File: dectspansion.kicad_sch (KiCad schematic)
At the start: 21 parts, among them J1 Hexpansion-Connector, J2 Conn_02x10_Odd_Even, J3 AudioJack4, U2 SC14CVMDECT

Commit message: Created PCB layout
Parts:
- removed D1: LED, LED_SMD:LED_0805_2012Metric, symbol Device:LED
- removed J2: Conn_02x10_Odd_Even, Connector_PinHeader_2.54mm:PinHeader_2x10_P2.54mm_Vertical, symbol Connector_Generic:Conn_02x10_Odd_Even
- removed R1: R, Resistor_SMD:R_0603_1608Metric, symbol Device:R
- renumbered D2 to D3
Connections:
- net 3V3 is gone; now on net +3V3: J1.15 (3V3), J1.16 (3V3)
- net HS_H: now also U2.47 (URX)
- net HS_I: now also U2.48 (UTX)
- net Mic: now also R10.1; no longer R10.2
- net at U2.7 (VREFp): now also R10.2; no longer R10.1
- net LS_A: no longer names the net of J1.2 (LS_A)
- net LS_B: no longer names the net of J1.3 (LS_B)
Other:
- moved on the sheet: C11, C12, C4, C5, C6, C9, D2, D3, J1, J3, JP1, R10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

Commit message: Created PCB layout
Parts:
- added J2: Conn_01x03_Pin, Connector_PinHeader_2.54mm:PinHeader_1x03_P2.54mm_Vertical, symbol Connector:Conn_01x03_Pin
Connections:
- net GND: now also J2.3 (Pin_3)
- net HS_H: now also J2.2 (Pin_2)
- net HS_I: now also J2.1 (Pin_1)
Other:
- moved on the sheet: J1

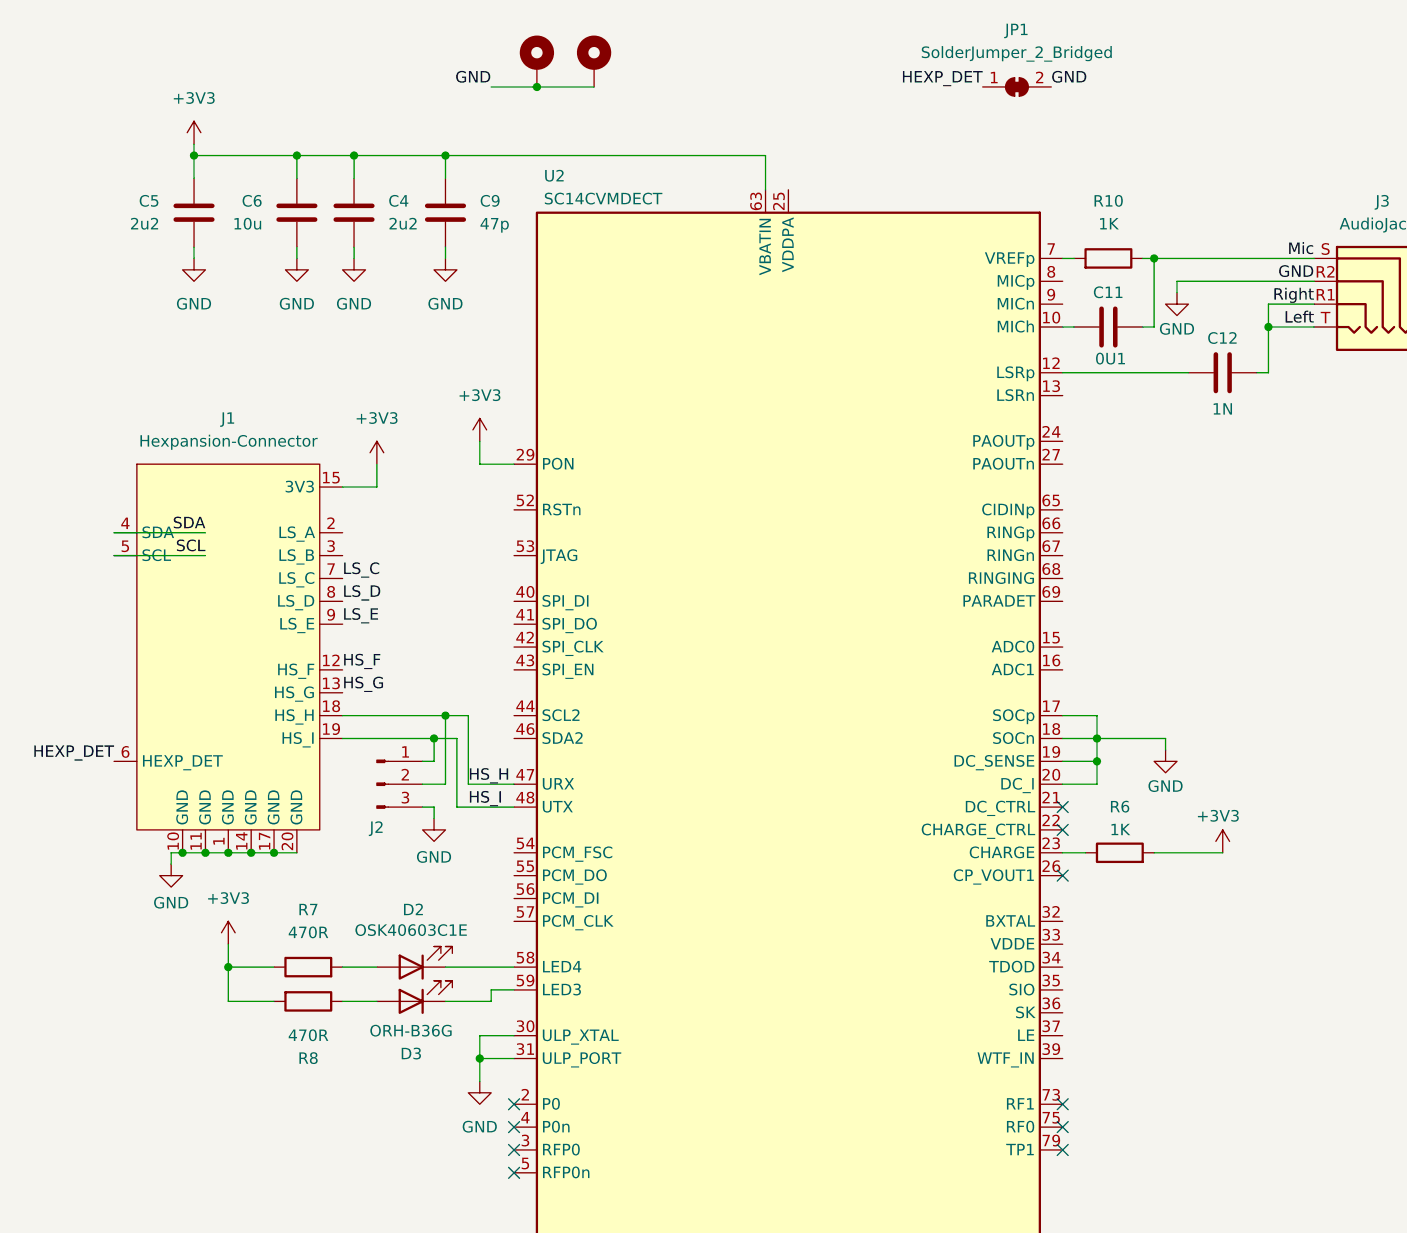
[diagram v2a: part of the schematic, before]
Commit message: Adjustments to schmatic, board layout, and added part list to readme
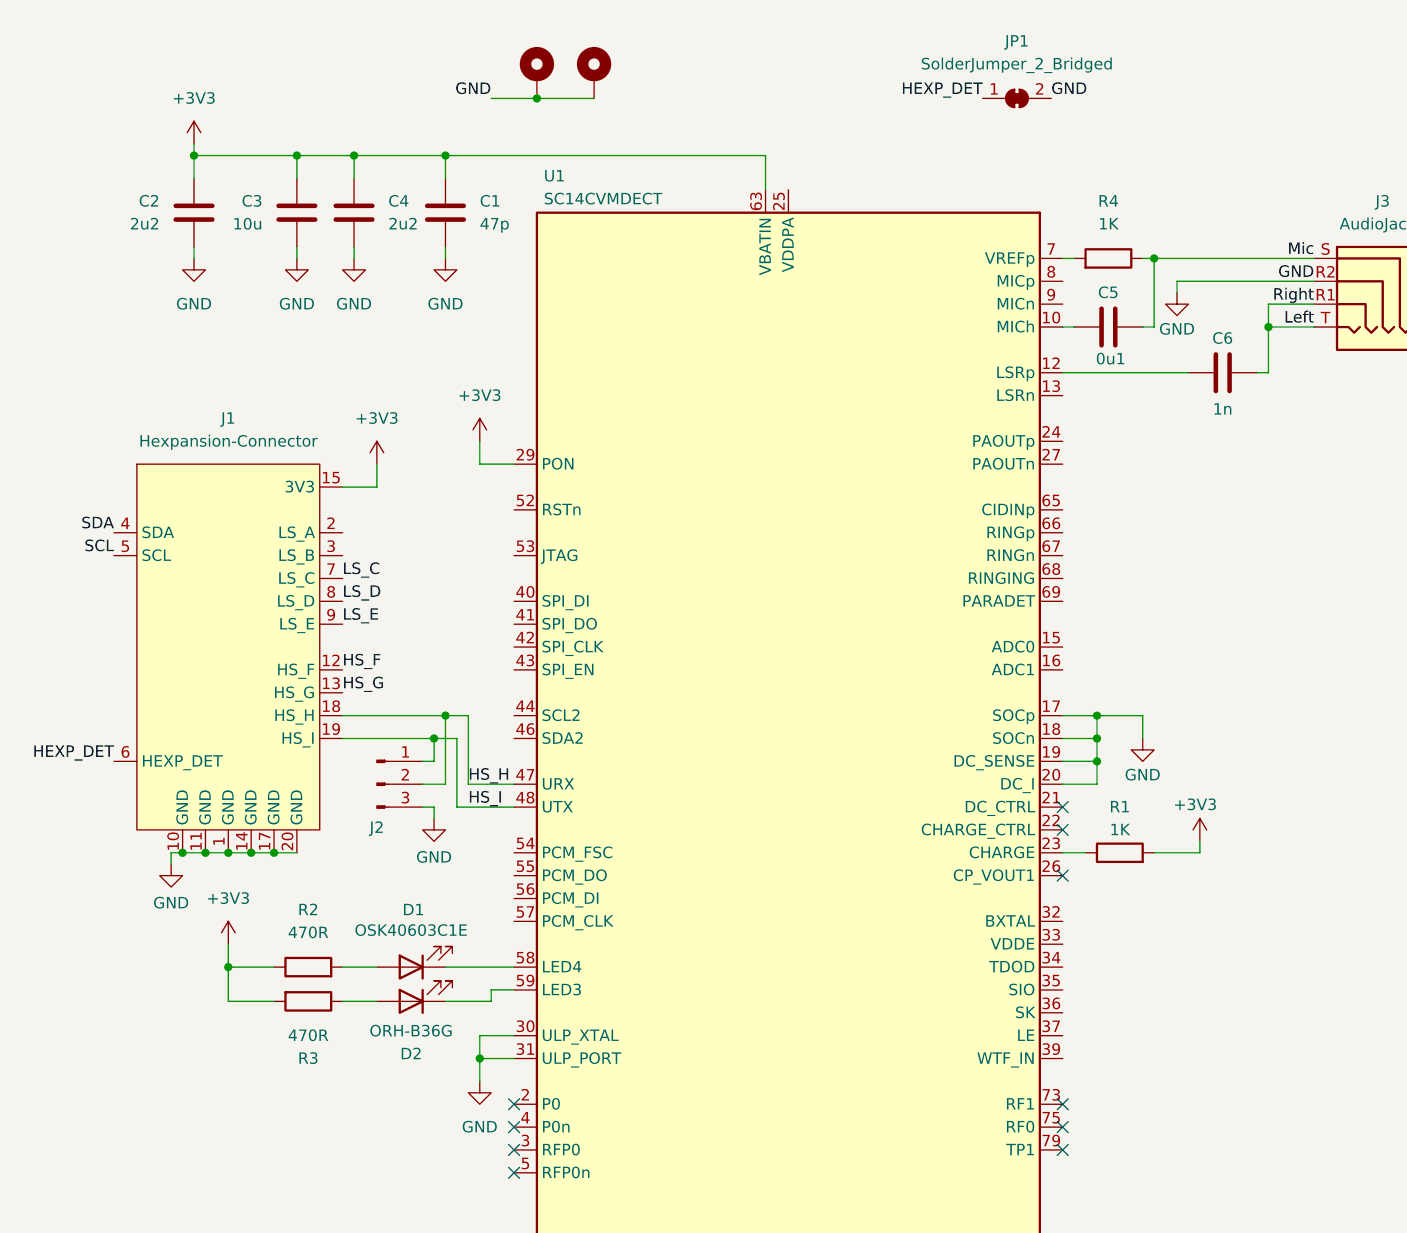
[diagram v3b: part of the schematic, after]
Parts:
- C5: renamed from C11; value 0U1 -> 0u1
- C6: renamed from C12; value 1N -> 1n
- renumbered C9 to C1, C5 to C2, C6 to C3, D2 to D1, D3 to D2, R6 to R1, R7 to R2, R8 to R3, R10 to R4, U2 to U1
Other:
- moved on the sheet: JP1

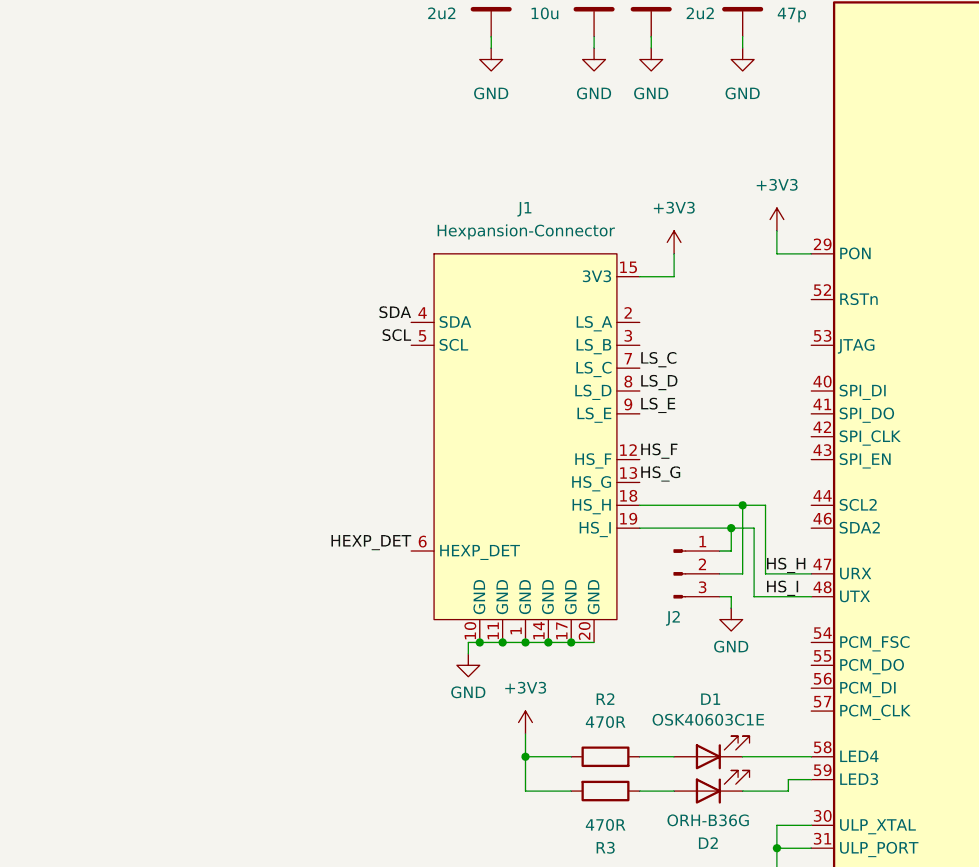
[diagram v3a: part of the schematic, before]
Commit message: Added uart level shifting
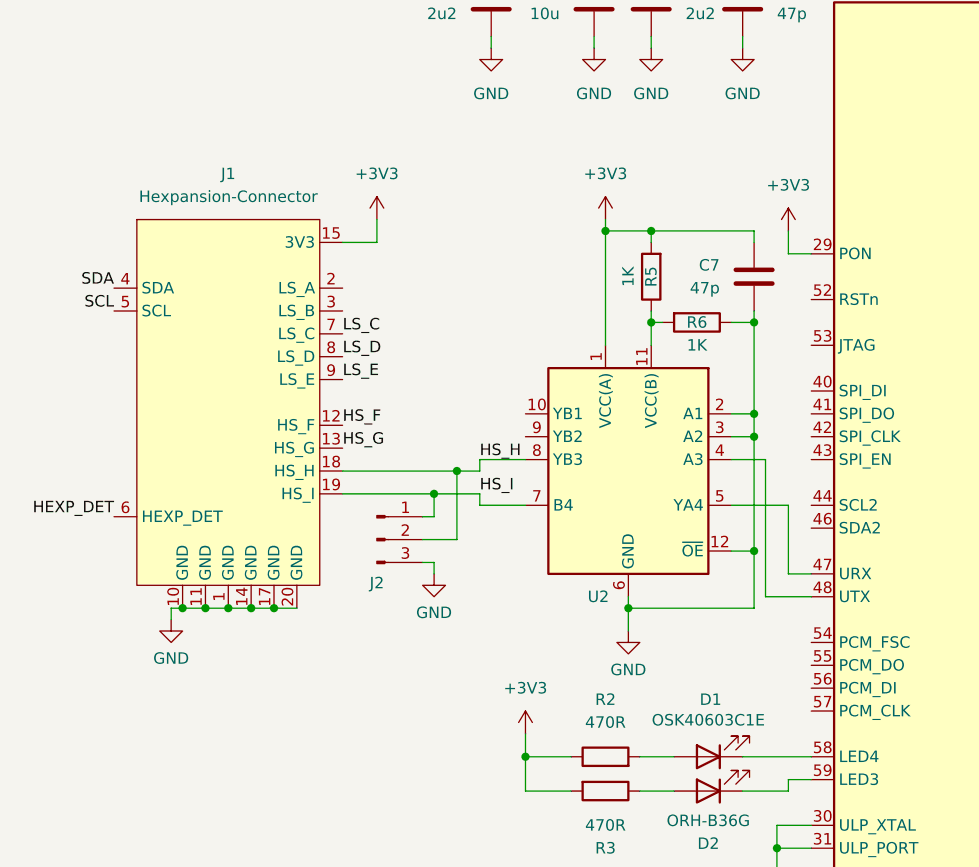
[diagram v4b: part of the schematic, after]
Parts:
- added C7: 47p, Capacitor_SMD:C_0603_1608Metric, symbol Device:C
- added R5, R6: 1K, Resistor_SMD:R_0603_1608Metric, symbol Device:R
- added U2: ~, 74AVC4T3144:74AVC4T3144, symbol 74AVC4T3144:74AVC4T3144
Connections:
- net +3V3: now also C7.1, R5.2, U2.1 (VCC(A))
- net GND: now also C7.2, R6.1, U2.12 (~{OE}), U2.2 (A1), U2.3 (A2), U2.6 (GND)
- net HS_H: now also U2.8 (YB3); no longer U1.47 (URX)
- net HS_I: now also U2.7 (B4); no longer U1.48 (UTX)
- new net: R5.1, R6.2, U2.11 (VCC(B))
- new net: U1.47 (URX), U2.5 (YA4)
- new net: U1.48 (UTX), U2.4 (A3)
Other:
- moved on the sheet: J1, J2

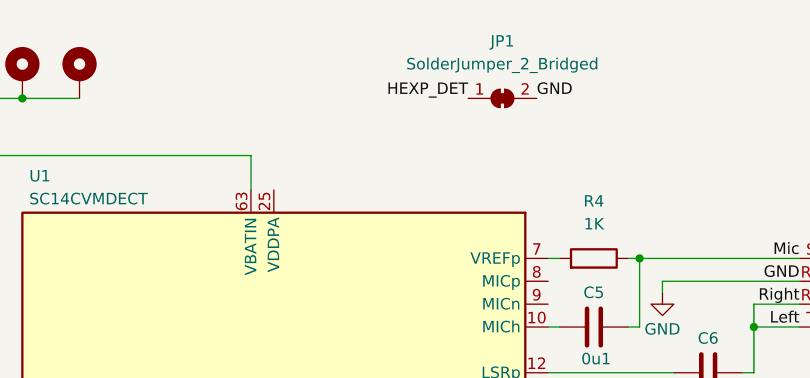
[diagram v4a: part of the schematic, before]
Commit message: Added level shifitng, updated schematic, layout and gerbers
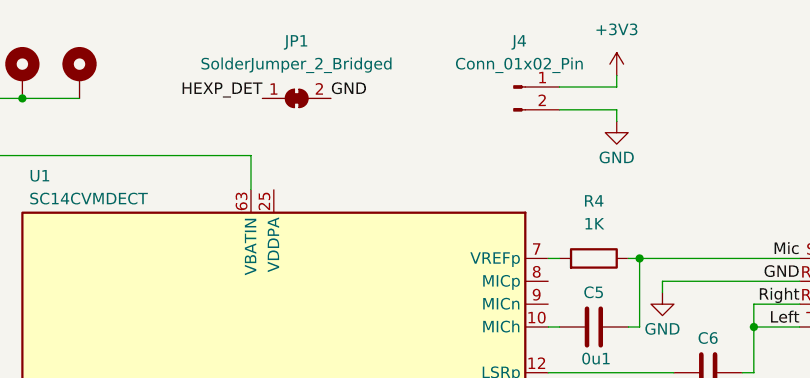
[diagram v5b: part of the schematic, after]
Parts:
- added J4: Conn_01x02_Pin, Connector_PinHeader_2.54mm:PinHeader_1x02_P2.54mm_Vertical, symbol Connector:Conn_01x02_Pin
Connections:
- net +3V3: now also J4.1 (Pin_1)
- net GND: now also J4.2 (Pin_2)
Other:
- title: (none) -> DECTspansion DECT Telephon Expansion Module
- moved on the sheet: JP1

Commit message: Fixed bug
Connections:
- net +3V3: now also U2.11 (VCC(B)); no longer U2.1 (VCC(A))
- net at R5.1, R6.2: now also U2.1 (VCC(A)); no longer U2.11 (VCC(B))
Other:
- moved on the sheet: R5, R6
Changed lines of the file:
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@@
 	)
 	(junction
-		(at 144.78 104.14)
+		(at 138.43 72.39)
 		(diameter 0)
 		(color 0 0 0 0)
 	)
 	(junction
-		(at 138.43 72.39)
+		(at 144.78 104.14)
 		(diameter 0)
 		(color 0 0 0 0)
@@
 	)
 	(junction
-		(at 156.21 114.3)
-		(diameter 0)
-		(color 0 0 0 0)
-	)
-	(junction
 		(at 97.79 146.05)
 		(diameter 0)
@@
 	)
 	(junction
-		(at 144.78 114.3)
+		(at 139.7 114.3)
 		(diameter 0)
 		(color 0 0 0 0)
@@
 	)
 	(junction
+		(at 156.21 114.3)
+		(diameter 0)
+		(color 0 0 0 0)
+	)
+	(junction
 		(at 123.19 130.81)
 		(diameter 0)
@@
 	)
 	(junction
-		(at 190.5 219.71)
+		(at 139.7 104.14)
 		(diameter 0)
 		(color 0 0 0 0)
 	)
 	(junction
-		(at 120.65 133.35)
+		(at 190.5 219.71)
 		(diameter 0)
 		(color 0 0 0 0)
 	)
 	(junction
-		(at 139.7 104.14)
+		(at 120.65 133.35)
 		(diameter 0)
 		(color 0 0 0 0)
@@
 	(wire
 		(pts
+			(xy 156.21 114.3) (xy 156.21 124.46)
+		)
+		(stroke
+			(width 0)
+			(type default)
+		)
+	)
+	(wire
+		(pts
 			(xy 119.38 135.89) (xy 120.65 135.89)
 		)
@@
 	(wire
 		(pts
+			(xy 139.7 114.3) (xy 147.32 114.3)
+		)
+		(stroke
+			(width 0)
+			(type default)
+		)
+	)
+	(wire
+		(pts
 			(xy 162.56 142.24) (xy 160.02 142.24)
 		)
@@
 	(wire
 		(pts
-			(xy 144.78 104.14) (xy 156.21 104.14)
-		)
-		(stroke
-			(width 0)
-			(type default)
-		)
-	)
-	(wire
-		(pts
 			(xy 251.46 88.9) (xy 246.38 88.9)
 		)
@@
 	(wire
 		(pts
-			(xy 144.78 104.14) (xy 144.78 105.41)
-		)
-		(stroke
-			(width 0)
-			(type default)
-		)
-	)
-	(wire
-		(pts
 			(xy 138.43 82.55) (xy 138.43 83.82)
 		)
@@
 	(wire
 		(pts
-			(xy 139.7 102.87) (xy 139.7 104.14)
-		)
-		(stroke
-			(width 0)
-			(type default)
-		)
-	)
-	(wire
-		(pts
 			(xy 156.21 124.46) (xy 153.67 124.46)
 		)
@@
 	(wire
 		(pts
-			(xy 156.21 114.3) (xy 156.21 124.46)
+			(xy 156.21 113.03) (xy 156.21 114.3)
 		)
 		(stroke
@@
 	(wire
 		(pts
+			(xy 144.78 104.14) (xy 144.78 116.84)
+		)
+		(stroke
+			(width 0)
+			(type default)
+		)
+	)
+	(wire
+		(pts
 			(xy 123.19 130.81) (xy 123.19 138.43)
 		)
@@
 	(wire
 		(pts
-			(xy 144.78 114.3) (xy 144.78 116.84)
+			(xy 139.7 114.3) (xy 139.7 116.84)
 		)
 		(stroke
@@
 	(wire
 		(pts
+			(xy 139.7 104.14) (xy 144.78 104.14)
+		)
+		(stroke
+			(width 0)
+			(type default)
+		)
+	)
+	(wire
+		(pts
 			(xy 138.43 72.39) (xy 144.78 72.39)
 		)
@@
 	(wire
 		(pts
-			(xy 160.02 66.04) (xy 165.1 66.04)
+			(xy 139.7 102.87) (xy 139.7 104.14)
 		)
 		(stroke
@@
 	(wire
 		(pts
-			(xy 193.04 219.71) (xy 193.04 218.44)
+			(xy 160.02 66.04) (xy 165.1 66.04)
 		)
 		(stroke
@@
 	(wire
 		(pts
-			(xy 110.49 130.81) (xy 123.19 130.81)
+			(xy 193.04 219.71) (xy 193.04 218.44)
 		)
 		(stroke
@@
 	(wire
 		(pts
-			(xy 246.38 91.44) (xy 251.46 91.44)
+			(xy 110.49 130.81) (xy 123.19 130.81)
 		)
 		(stroke
@@
 	(wire
 		(pts
-			(xy 238.76 149.86) (xy 233.68 149.86)
+			(xy 246.38 91.44) (xy 251.46 91.44)
 		)
 		(stroke
@@
 	(wire
 		(pts
-			(xy 139.7 104.14) (xy 139.7 116.84)
+			(xy 238.76 149.86) (xy 233.68 149.86)
 		)
 		(stroke
@@
 	(wire
 		(pts
-			(xy 156.21 113.03) (xy 156.21 114.3)
+			(xy 154.94 114.3) (xy 156.21 114.3)
 		)
 		(stroke
@@
 	(wire
 		(pts
-			(xy 144.78 113.03) (xy 144.78 114.3)
-		)
-		(stroke
-			(width 0)
-			(type default)
-		)
-	)
-	(wire
-		(pts
 			(xy 123.19 138.43) (xy 119.38 138.43)
 		)
@@
 	(wire
 		(pts
-			(xy 139.7 104.14) (xy 144.78 104.14)
+			(xy 91.44 146.05) (xy 92.71 146.05)
 		)
 		(stroke
@@
 	(wire
 		(pts
-			(xy 91.44 146.05) (xy 92.71 146.05)
+			(xy 227.33 134.62) (xy 227.33 137.16)
 		)
 		(stroke
@@
 	(wire
 		(pts
-			(xy 227.33 134.62) (xy 227.33 137.16)
+			(xy 110.49 133.35) (xy 120.65 133.35)
 		)
 		(stroke
@@
 	(wire
 		(pts
-			(xy 144.78 114.3) (xy 146.05 114.3)
+			(xy 144.78 72.39) (xy 154.94 72.39)
 		)
 		(stroke
@@
 	(wire
 		(pts
-			(xy 110.49 133.35) (xy 120.65 133.35)
+			(xy 160.02 106.68) (xy 162.56 106.68)
 		)
 		(stroke
@@
 	(wire
 		(pts
-			(xy 144.78 72.39) (xy 154.94 72.39)
+			(xy 120.65 133.35) (xy 125.73 133.35)
 		)
 		(stroke
@@
 	(wire
 		(pts
-			(xy 160.02 106.68) (xy 162.56 106.68)
+			(xy 143.51 166.37) (xy 147.32 166.37)
 		)
 		(stroke
@@
 	(wire
 		(pts
-			(xy 120.65 133.35) (xy 125.73 133.35)
+			(xy 153.67 127) (xy 156.21 127)
 		)
 		(stroke
@@
 	(wire
 		(pts
-			(xy 143.51 166.37) (xy 147.32 166.37)
+			(xy 153.67 139.7) (xy 156.21 139.7)
 		)
 		(stroke
@@
 	(wire
 		(pts
-			(xy 153.67 127) (xy 156.21 127)
+			(xy 139.7 113.03) (xy 139.7 114.3)
 		)
 		(stroke
@@
 	(wire
 		(pts
-			(xy 153.67 114.3) (xy 156.21 114.3)
+			(xy 142.24 144.78) (xy 142.24 146.05)
 		)
 		(stroke
@@
 	(wire
 		(pts
-			(xy 153.67 139.7) (xy 156.21 139.7)
+			(xy 190.5 219.71) (xy 190.5 218.44)
 		)
 		(stroke
@@
 	(wire
 		(pts
-			(xy 142.24 144.78) (xy 142.24 146.05)
+			(xy 143.51 162.56) (xy 147.32 162.56)
 		)
 		(stroke
@@
 	(wire
 		(pts
-			(xy 190.5 219.71) (xy 190.5 218.44)
+			(xy 144.78 104.14) (xy 156.21 104.14)
 		)
 		(stroke
@@
 	(wire
 		(pts
-			(xy 143.51 162.56) (xy 147.32 162.56)
+			(xy 139.7 104.14) (xy 139.7 105.41)
 		)
 		(stroke
@@
 	(symbol
 		(lib_id "Device:R")
-		(at 144.78 109.22 180)
+		(at 139.7 109.22 180)
 		(unit 1)
 		(exclude_from_sim no)
@@
 		(dnp no)
 		(property "Reference" "R5"
-			(at 144.78 109.22 90)
+			(at 139.7 109.22 90)
 			(effects
 				(font
@@
 		)
 		(property "Value" "1K"
-			(at 142.24 109.22 90)
+			(at 137.16 109.22 90)
 			(effects
 				(font
@@
 		)
 		(property "Footprint" "Resistor_SMD:R_0603_1608Metric"
-			(at 146.558 109.22 90)
+			(at 141.478 109.22 90)
 			(effects
 				(font
@@
 		)
 		(property "Datasheet" "~"
-			(at 144.78 109.22 0)
+			(at 139.7 109.22 0)
 			(effects
 				(font
@@
 		)
 		(property "Description" "Resistor"
-			(at 144.78 109.22 0)
+			(at 139.7 109.22 0)
 			(effects
 				(font
@@
 	(symbol
 		(lib_id "Device:R")
-		(at 149.86 114.3 270)
+		(at 151.13 114.3 270)
 		(unit 1)
 		(exclude_from_sim no)
@@
 		(dnp no)
 		(property "Reference" "R6"
-			(at 149.86 114.3 90)
+			(at 151.13 114.3 90)
 			(effects
 				(font
@@
 		)
 		(property "Value" "1K"
-			(at 149.86 116.84 90)
+			(at 151.13 116.84 90)
 			(effects
 				(font
@@
 		)
 		(property "Footprint" "Resistor_SMD:R_0603_1608Metric"
-			(at 149.86 112.522 90)
+			(at 151.13 112.522 90)
 			(effects
 				(font
@@
 		)
 		(property "Datasheet" "~"
-			(at 149.86 114.3 0)
+			(at 151.13 114.3 0)
 			(effects
 				(font
@@
 		)
 		(property "Description" "Resistor"
-			(at 149.86 114.3 0)
+			(at 151.13 114.3 0)
 			(effects
 				(font
